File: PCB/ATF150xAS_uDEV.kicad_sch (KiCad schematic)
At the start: 16 parts, among them J1 Conn_02x05_Odd_Even, J2 VERT, J3 VERT, U1 ATF1502AS-xAx44

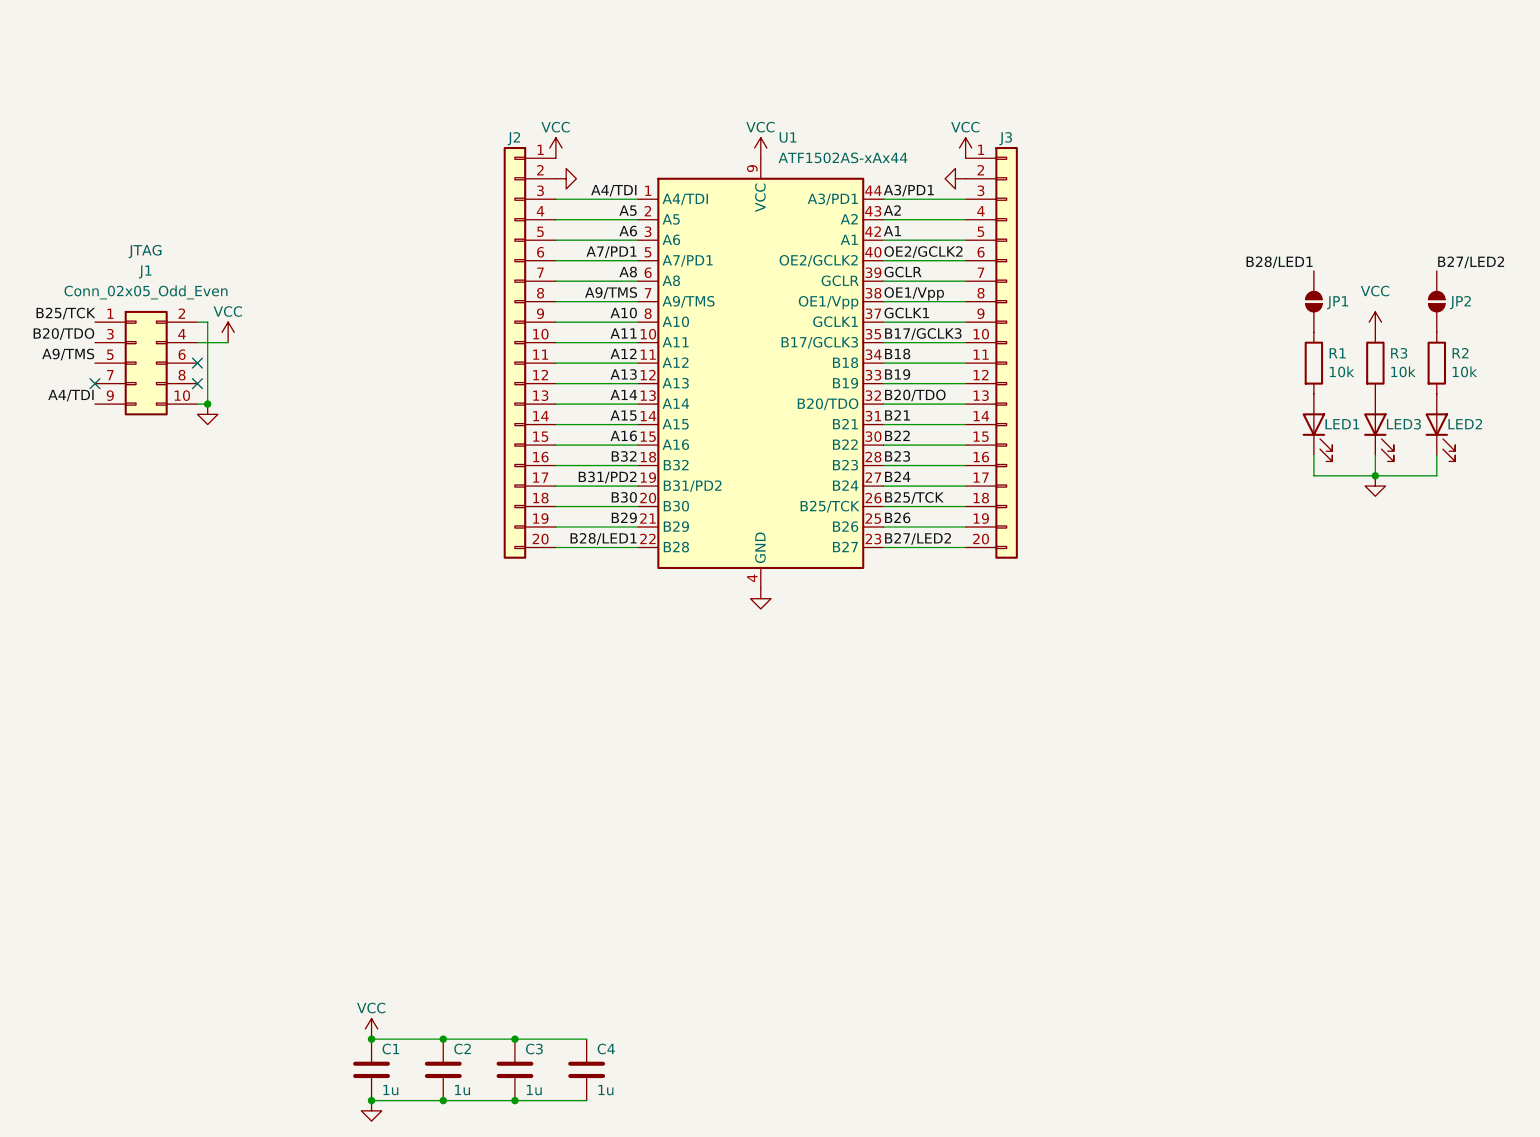
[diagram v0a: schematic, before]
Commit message: single board, silkscreen pin numbers
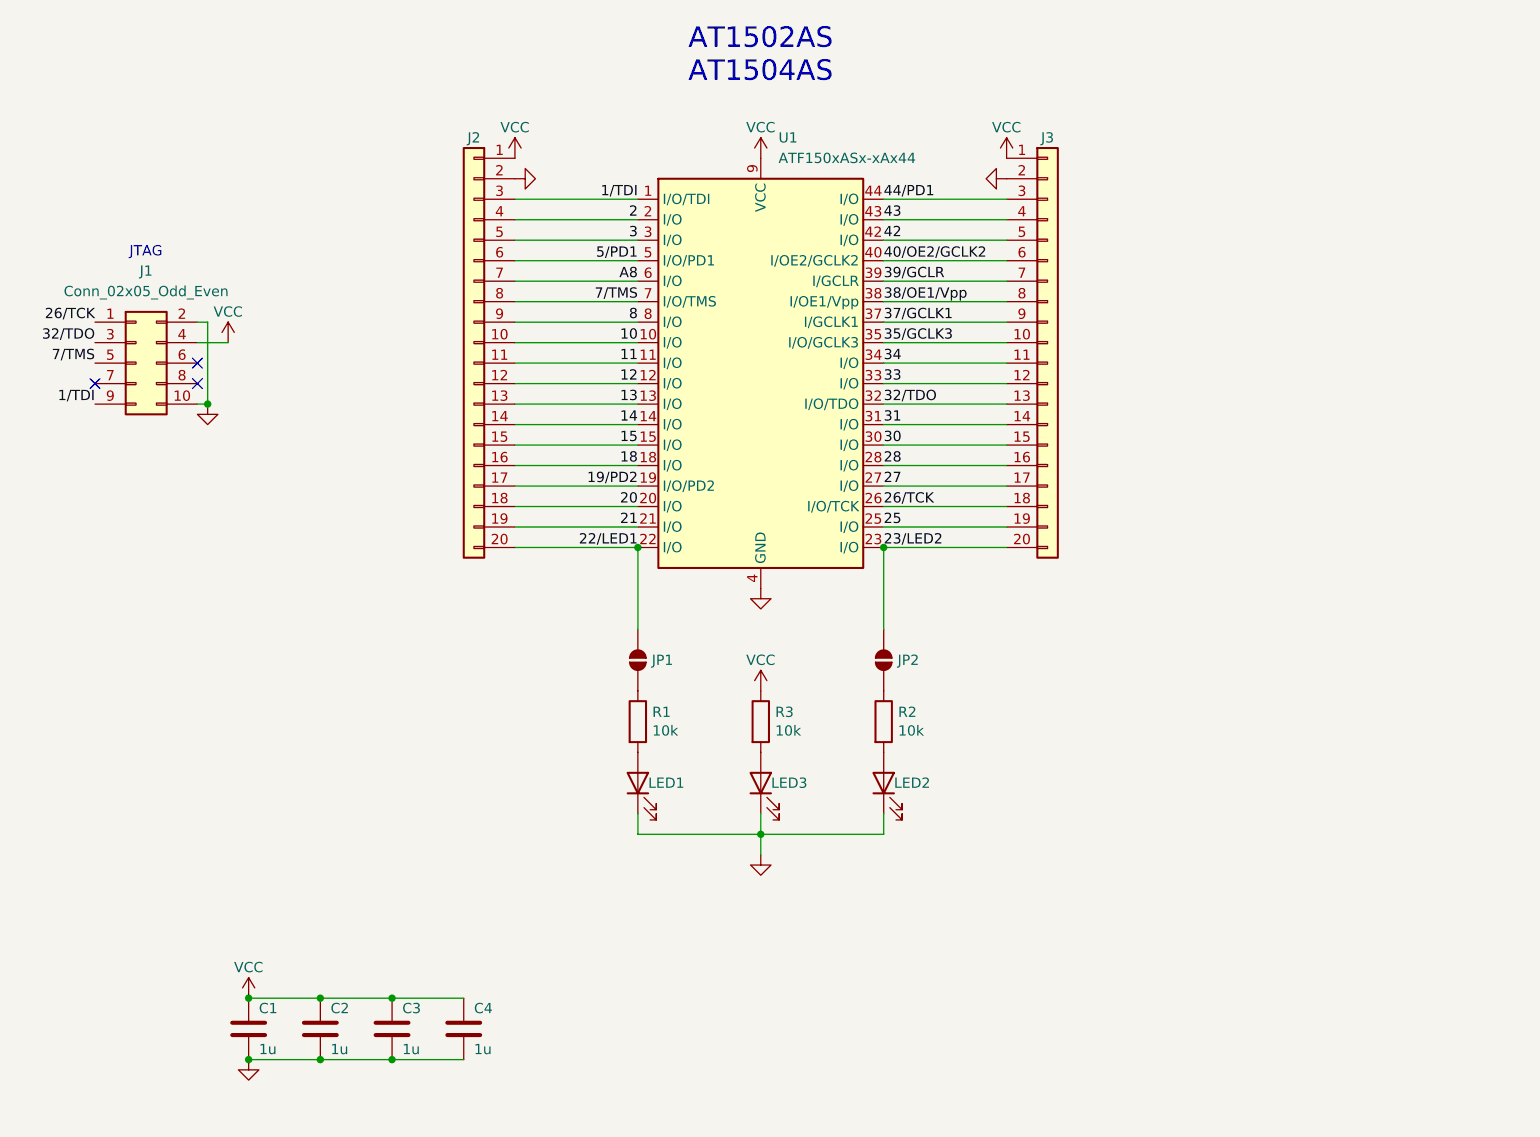
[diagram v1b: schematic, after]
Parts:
- removed U1: ATF1502AS-xAx44, 000_LOCAL:VQFP44, symbol 000_LOCAL:ATF1502AS-xAx44
- added U1: ATF150xASx-xAx44, 000_LOCAL:VQFP44, symbol 000_LOCAL:ATF150xASx-xAx44
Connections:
- net A8: now also U1.6 (I/O)
- net GND: now also U1.16 (GND), U1.24 (GND), U1.36 (GND), U1.4 (GND)
- net VCC: now also U1.17 (VCC), U1.29 (VCC), U1.41 (VCC), U1.9 (VCC)
- net A1 renamed 42
- net 42: now also U1.42 (I/O)
- net A10 renamed 8
- net 8: now also U1.8 (I/O)
- net A11 renamed 10
- net 10: now also U1.10 (I/O)
- net A12 renamed 11
- net 11: now also U1.11 (I/O)
- net A13 renamed 12
- net 12: now also U1.12 (I/O)
- net A14 renamed 13
- net 13: now also U1.13 (I/O)
- net A15 renamed 14
- net 14: now also U1.14 (I/O)
- net A16 renamed 15
- net 15: now also U1.15 (I/O)
- net A2 renamed 43
- net 43: now also U1.43 (I/O)
- net A3/PD1 renamed 44/PD1
- net 44/PD1: now also U1.44 (I/O)
- net A4/TDI renamed 1/TDI
- net 1/TDI: now also U1.1 (I/O/TDI)
- net A5 renamed 2
- net 2: now also U1.2 (I/O)
- net A6 renamed 3
- net 3: now also U1.3 (I/O)
- net A7/PD1 renamed 5/PD1
- net 5/PD1: now also U1.5 (I/O/PD1)
- net A9/TMS renamed 7/TMS
- net 7/TMS: now also U1.7 (I/O/TMS)
- net B17/GCLK3 renamed 35/GCLK3
- net 35/GCLK3: now also U1.35 (I/O/GCLK3)
- net B18 renamed 34
- net 34: now also U1.34 (I/O)
- net B19 renamed 33
- net 33: now also U1.33 (I/O)
- net B20/TDO renamed 32/TDO
- net 32/TDO: now also U1.32 (I/O/TDO)
- net B21 renamed 31
- net 31: now also U1.31 (I/O)
- net B22 renamed 30
- net 30: now also U1.30 (I/O)
- net B23 renamed 28
- net 28: now also U1.28 (I/O)
- net B24 renamed 27
- net 27: now also U1.27 (I/O)
- net B25/TCK renamed 26/TCK
- net 26/TCK: now also U1.26 (I/O/TCK)
- net B26 renamed 25
- net 25: now also U1.25 (I/O)
- net B27/LED2 renamed 23/LED2
- net 23/LED2: now also U1.23 (I/O)
- net B28/LED1 renamed 22/LED1
- net 22/LED1: now also U1.22 (I/O)
- net B29 renamed 21
- net 21: now also U1.21 (I/O)
- net B30 renamed 20
- net 20: now also U1.20 (I/O)
- net B31/PD2 renamed 19/PD2
- net 19/PD2: now also U1.19 (I/O/PD2)
- net B32 renamed 18
- net 18: now also U1.18 (I/O)
- net GCLK1 renamed 37/GCLK1
- net 37/GCLK1: now also U1.37 (I/GCLK1)
- net GCLR renamed 39/GCLR
- net 39/GCLR: now also U1.39 (I/GCLR)
- net OE1/Vpp renamed 38/OE1/Vpp
- net 38/OE1/Vpp: now also U1.38 (I/OE1/Vpp)
- net OE2/GCLK2 renamed 40/OE2/GCLK2
- net 40/OE2/GCLK2: now also U1.40 (I/OE2/GCLK2)
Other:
- note added: "AT1502AS AT1504AS"
- title: ATF1502AS_uDEV -> ATF150xAS_uDEV
- moved on the sheet: C1, C2, C3, C4, J2, J3, JP1, JP2, LED1, LED2, LED3, R1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
